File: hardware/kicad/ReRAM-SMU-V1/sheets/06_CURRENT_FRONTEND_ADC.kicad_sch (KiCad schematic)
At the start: 3 parts, among them U1 ADA4522 front-end PRIMARY 5uV, U2 OPA140 JFET for 100k/1M 10pA, U3 ADS1262 PRIMARY QFP-28 intern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

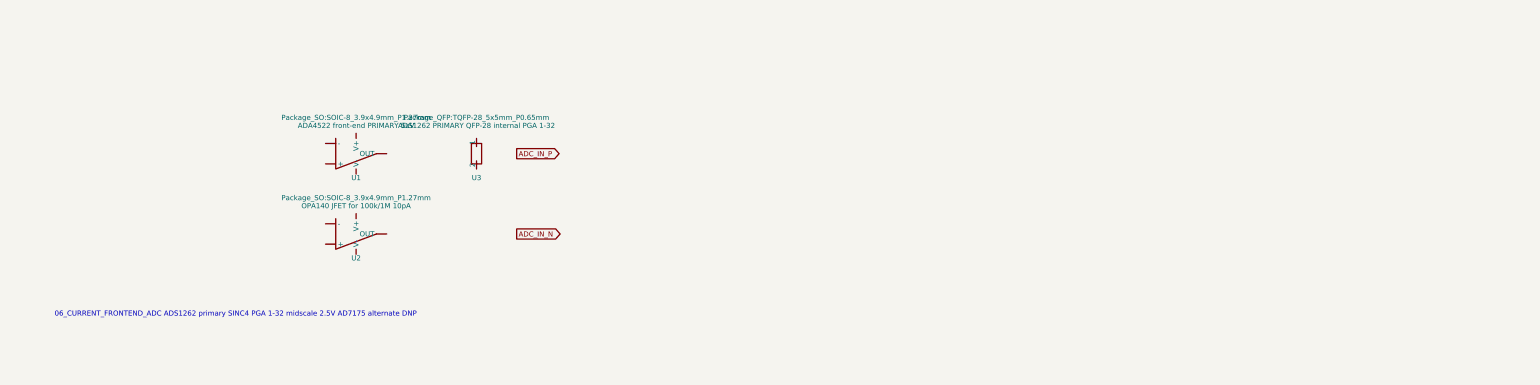
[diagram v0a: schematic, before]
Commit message: hardware: pre-ERC manufacturer corrections (LT1970 physical pins, ADS1262 TSSOP-28, MCU G431RBT6, 74LVC1G74 latch, LT5400 Kelvin, AD5764 rails, ADS1262 bipolar)
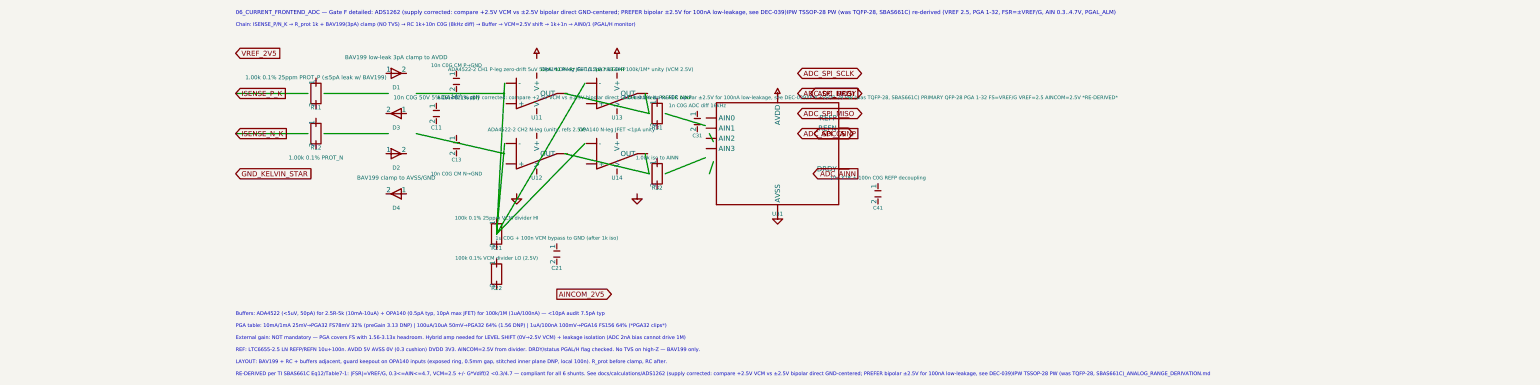
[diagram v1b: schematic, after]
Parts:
- removed U1: ADA4522 front-end PRIMARY 5uV, Package_SO:SOIC-8_3.9x4.9mm_P1.27mm, symbol Device:OpAmp
- removed U2: OPA140 JFET for 100k/1M 10pA, Package_SO:SOIC-8_3.9x4.9mm_P1.27mm, symbol Device:OpAmp
- removed U3: ADS1262 PRIMARY QFP-28 internal PGA 1-32, Package_QFP:TQFP-28_5x5mm_P0.65mm, symbol Device:R
- added C11: 10n C0G 50V 5% DA<0.1% diff, Capacitor_SMD:C_0805_2012Metric, symbol Device:C
- added C12: 10n C0G CM P→GND, symbol Device:C
- added C13: 10n C0G CM N→GND, symbol Device:C
- added C21: 1u C0G + 100n VCM bypass to GND (after 1k iso), symbol Device:C
- added C31: 1n C0G ADC diff 16kHz, symbol Device:C
- added C41: 10u X7R + 100n C0G REFP decoupling, symbol Device:C
- added D1: BAV199 low-leak 3pA clamp to AVDD, Diode_SMD:D_SOT-23, symbol Device:D
- added D2: BAV199 clamp to AVSS/GND, symbol Device:D
- added D3: BAV199 N-leg to AVDD, symbol Device:D
- added D4: BAV199 N-leg to AVSS, symbol Device:D
- added R11: 1.00k 0.1% 25ppm PROT_P (≤5pA leak w/ BAV199), Resistor_SMD:R_0805_2012Metric, symbol Device:R
- added R12: 1.00k 0.1% PROT_N, symbol Device:R
- added R21: 100k 0.1% 25ppm VCM divider HI, symbol Device:R
- added R22: 100k 0.1% VCM divider LO (2.5V), symbol Device:R
- added R31: 1.00k 0.1% iso to ADC AINP, symbol Device:R
- added R32: 1.00k iso to AINN, symbol Device:R
- added U11: ADA4522-2 CH1 P-leg zero-drift 5uV 50pA *LOW-R* G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, symbol Custom:ADA4522
- added U12: ADA4522-2 CH2 N-leg (unity, refs 2.5V), symbol Custom:ADA4522
- added U13: OPA140 P-leg JFET 0.5pA *HIGH-R 100k/1M* unity (V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, Package_SO:SOIC-8_3.9x4.9mm_P1.27mm, symbol Custom:OPA140
- added U14: OPA140 N-leg JFET <1pA unity, symbol Custom:OPA140
- added U31: ADS1262 (supply corrected: compare +2.5V VCM vs ±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, symbol Custom:ADS1262 (supply corrected: compare +2.5V VCM vs ±2.5V bipolar direct GND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
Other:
- note added: "06_CURRENT_FRONTEND_ADC — Gate F detailed: ADS1262 (supply corrected: compare +2.5V VCM vs ±2.5V bipolar direct GND-centered; PREFER bipolar ±2.5V for 100nA low-leakage, see DEC-039)IPW TSSOP-28 PW (was TQFP-28, SBAS661C) re-derived (VREF 2.5, PGA 1-32, FSR=±VREF/G, AIN 0.3..4.7V, PGAL_ALM)"
- note added: "Buffers: ADA4522 (<5uV, 50pA) for 2.5R-5k (10mA-10uA) + OPA140 (0.5pA typ, 10pA max JFET) for 100k/1M (1uA/100nA) — <10pA audit 7.5pA typ"
- note added: "Chain: ISENSE_P/N_K → R_prot 1k + BAV199(3pA) clamp (NO TVS) → RC 1k+10n C0G (8kHz diff) → Buffer → VCM=2.5V shift → 1k+1n → AIN0/1 (PGAL/H monitor)"
- note added: "External gain: NOT mandatory — PGA covers FS with 1.56-3.13x headroom. Hybrid amp needed for LEVEL SHIFT (0V→2.5V VCM) + leakage isolation (ADC 2nA bias cannot drive 1M)"
- note added: "LAYOUT: BAV199 + RC + buffers adjacent, guard keepout on OPA140 inputs (exposed ring, 0.5mm gap, stitched inner plane DNP, local 100n). R_prot before clamp, RC after."
- note added: "PGA table: 10mA/1mA 25mV→PGA32 FS78mV 32% (preGain 3.13 DNP) | 100uA/10uA 50mV→PGA32 64% (1.56 DNP) | 1uA/100nA 100mV→PGA16 FS156 64% (*PGA32 clips*)"
- note added: "RE-DERIVED per TI SBAS661C Eq12/Table7-1: |FSR|=VREF/G, 0.3<=AIN<=4.7, VCM=2.5 +/- G*Vdiff/2 <0.3/4.7 — compliant for all 6 shunts. See docs/calculations/ADS1262 (supply corrected: compare +2.5V VCM vs ±2.5V bipolar direct GND-centered; PREFER bipolar ±2.5V for 100nA low-leakage, see DEC-039)IPW TSSOP-28 PW (was TQFP-28, SBAS661C)_ANALOG_RANGE_DERIVATION.md"
- note added: "REF: LTC6655-2.5 LN REFP/REFN 10u+100n. AVDD 5V AVSS 0V (0.3 cushion) DVDD 3V3. AINCOM=2.5V from divider. DRDY/status PGAL/H flag checked. No TVS on high-Z — BAV199 only."
- note removed: "06_CURRENT_FRONTEND_ADC ADS1262 primary SINC4 PGA 1-32 midscale 2.5V AD7175 alternate DNP"
- company: ReRAM-SMU V1 -> ReRAM-SMU V1 — Gate F detailed

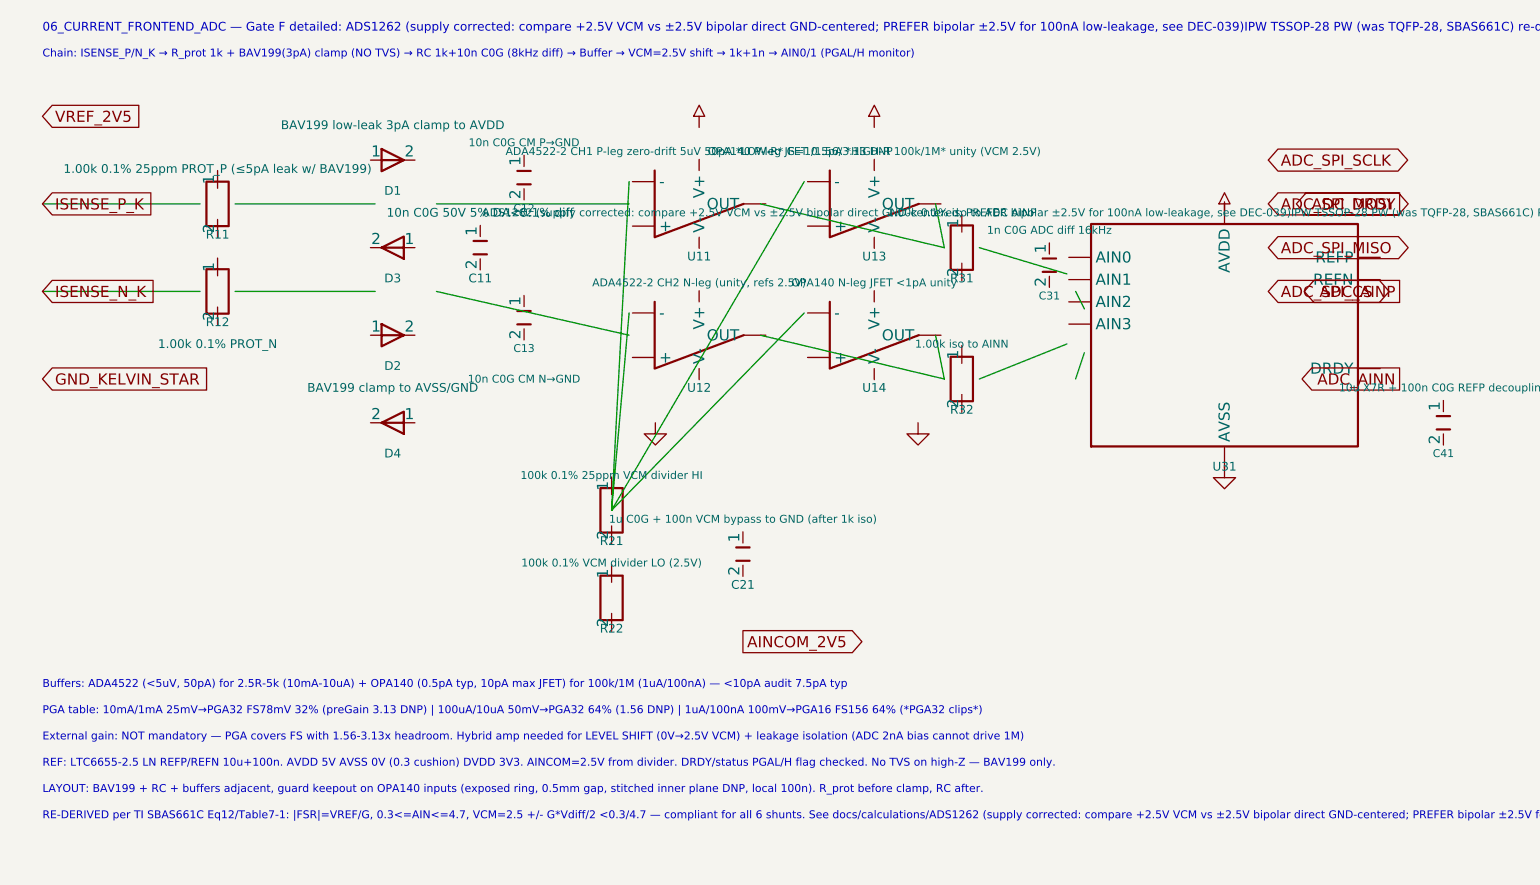
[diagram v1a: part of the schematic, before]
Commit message: hardware: pre-ERC correction gate 2 (LT1970 consistency, LT5400A-1 MSOP-8, ADS1262IPW 28-pin, bipolar ±2.5V, buffer per-range, power baseline normalize)
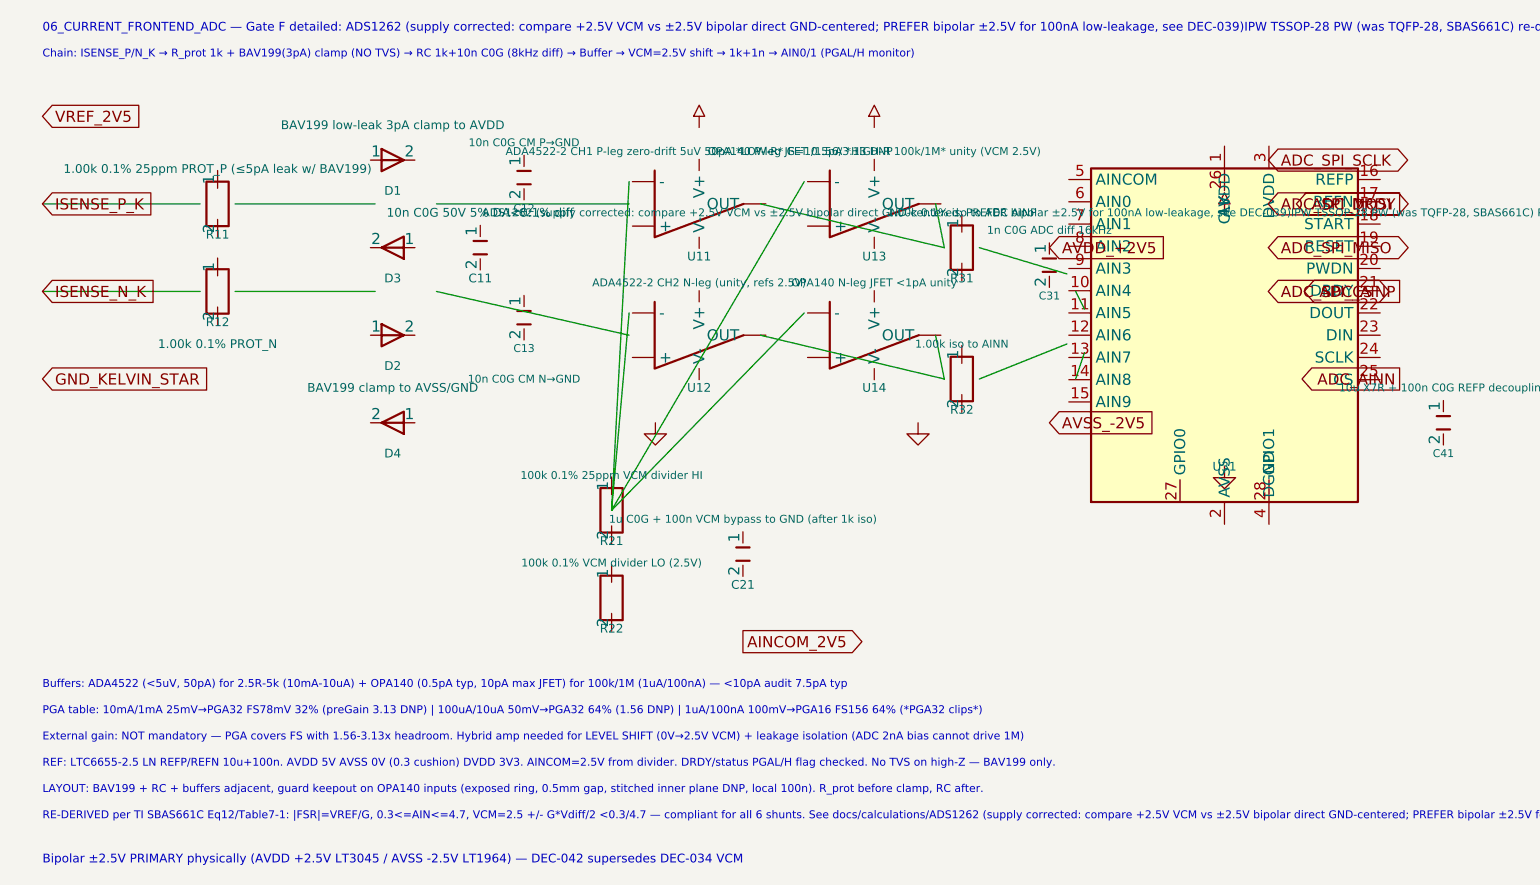
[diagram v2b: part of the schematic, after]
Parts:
- U31: symbol Custom:ADS1262 (supply corrected: compare +2.5V VCM vs ±2.5V bipolar direct GND-centered; PREFER bipolar ±2.5V for 100n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 -> ReRAM_SMU:ADS1262IPW
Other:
- note added: "Bipolar ±2.5V PRIMARY physically (AVDD +2.5V LT3045 / AVSS -2.5V LT1964) — DEC-042 supersedes DEC-034 VCM"
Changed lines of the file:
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@@
 	)
 	; --- ADS1262 (supply corrected: compare +2.5V VCM vs ±2.5V bipolar direct GND-centered; PREFER bipolar ±2.5V for 100nA low-leakage, see DEC-039)IPW TSSOP-28 PW (was TQFP-28, SBAS661C) primary ---
-	(symbol (lib_id "Custom:ADS1262 (supply corrected: compare +2.5V VCM vs ±2.5V bipolar direct GND-centered; PREFER bipolar ±2.5V for 100nA low-leakage, see DEC-039)IPW TSSOP-28 PW (was TQFP-28, SBAS661C)") (at 145 40 0) (unit 1) (exclude_from_sim no) (in_bom yes) (on_board yes) (dnp no)
+	(symbol (lib_id "ReRAM_SMU:ADS1262IPW") (at 145 40 0) (unit 1) (exclude_from_sim no) (in_bom yes) (on_board yes) (dnp no)
 		(uuid "u-ads1262") (property "Reference" "U31" (at 145 55 0) (effects (font (size 1.0 1.0))))
 		(property "Value" "ADS1262 (supply corrected: compare +2.5V VCM vs ±2.5V bipolar direct GND-centered; PREFER bipolar ±2.5V for 100nA low-leakage, see DEC-039)IPW TSSOP-28 PW (was TQFP-28, SBAS661C) PRIMARY QFP-28 PGA 1-32 FS=VREF/G VREF=2.5 AINCOM=2.5V *RE-DERIVED*" (at 145 26 0) (effects (font (size 0.9 0.9))))
@@
 	(global_label "ADC_DRDY" (shape output) (at 165 25 180) (fields_autoplaced yes) (uuid "drdy"))
 	; --- Wires: Kelvin -> PROT -> RC -> Buffers -> iso -> ADC ---
-	(wire (pts (xy 10 25) (xy 28 25)) (stroke (width 0.254) (type default)) (uuid "w-p-kelvin"))
+	(global_label "AVDD_+2V5" (shape input) (at 125.0 30.0 0) (uuid "avdd25-glob") (property "Intersheetrefs" "${INTERSHEET_REFS}"))
+	(global_label "AVSS_-2V5" (shape input) (at 125.0 50.0 0) (uuid "avss25-glob") (property "Intersheetrefs" "${INTERSHEET_REFS}"))
+	(text "Bipolar ±2.5V PRIMARY physically (AVDD +2.5V LT3045 / AVSS -2.5V LT1964) — DEC-042 supersedes DEC-034 VCM" (at 10 100 0) (effects (font (size 1 1)) (justify left)))
+(wire (pts (xy 10 25) (xy 28 25)) (stroke (width 0.254) (type default)) (uuid "w-p-kelvin"))
 	(wire (pts (xy 10 35) (xy 28 35)) (stroke (width 0.254) (type default)) (uuid "w-n-kelvin"))
 	; R prot
